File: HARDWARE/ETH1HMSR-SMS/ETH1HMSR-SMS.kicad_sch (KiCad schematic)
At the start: 5 parts

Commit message: SW and HW development
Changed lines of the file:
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@@
     )
   )
-  (sheet (at 122.555 99.06) (size 104.14 30.48) (fields_autoplaced)
+  (sheet (at 84.455 99.06) (size 142.24 30.48) (fields_autoplaced)
     (stroke (width 0.1524) (type solid))
     (fill (color 0 0 0 0.0000))
-    (property "Sheetname" "Power" (at 122.555 98.3484 0)
+    (property "Sheetname" "Power" (at 84.455 98.3484 0)
       (effects (font (size 1.27 1.27)) (justify left bottom))
     )
-    (property "Sheetfile" "Power.kicad_sch" (at 122.555 130.1246 0)
+    (property "Sheetfile" "Power.kicad_sch" (at 84.455 130.1246 0)
       (effects (font (size 1.27 1.27)) (justify left top))
     )

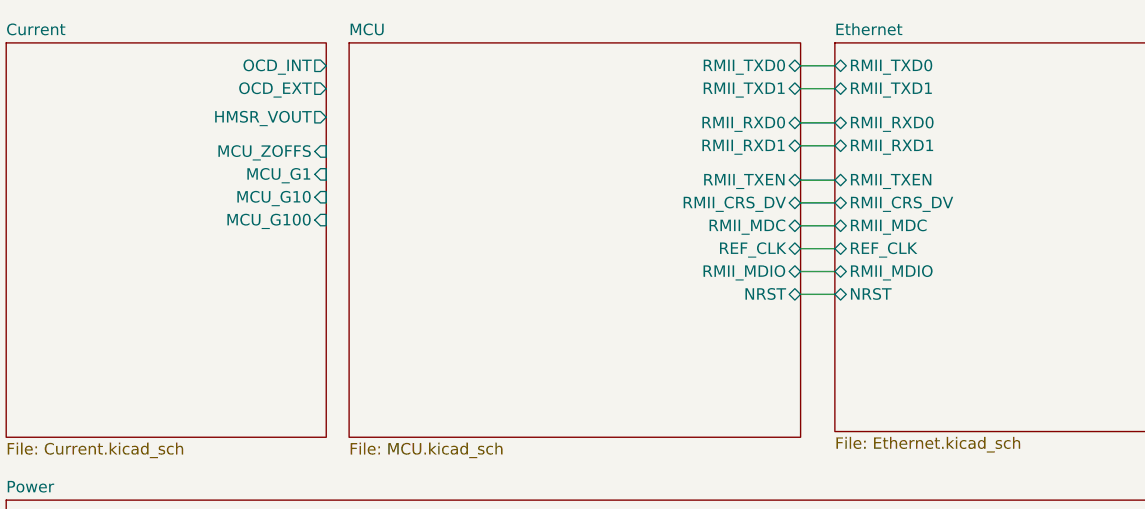
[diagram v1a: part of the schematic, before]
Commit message: Updated to Kicad 8
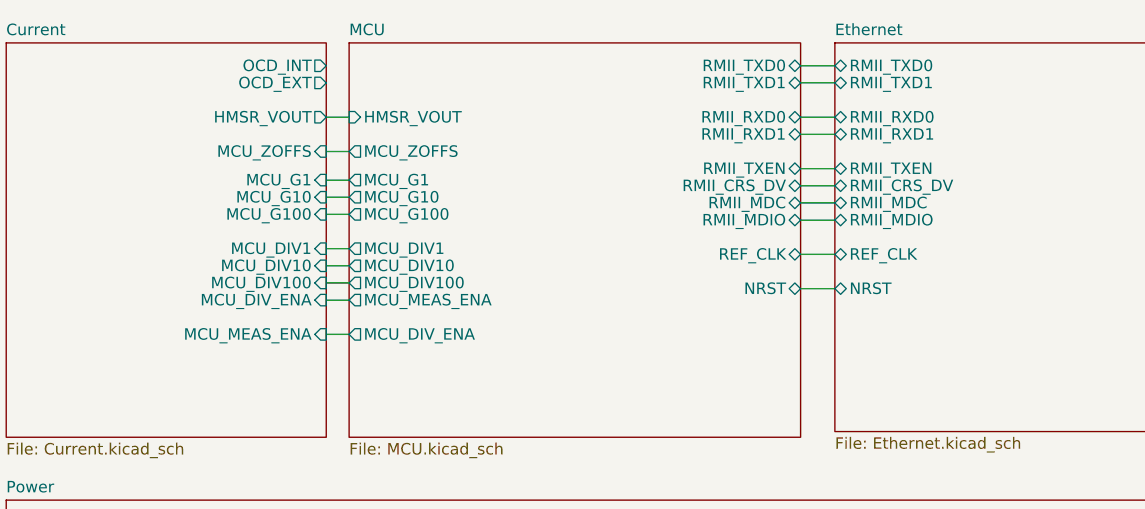
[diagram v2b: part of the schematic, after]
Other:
- sheet Current ports: added MCU_DIV1, MCU_DIV10, MCU_DIV100, MCU_DIV_ENA, MCU_MEAS_ENA; removed none
- sheet MCU ports: added HMSR_VOUT, MCU_DIV1, MCU_DIV10, MCU_DIV100, MCU_DIV_ENA, MCU_G1, MCU_G10, MCU_G100, MCU_MEAS_ENA, MCU_ZOFFS; removed none

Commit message: Development
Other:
- sheet MCU ports: added OCD_EXT, OCD_INT; removed none

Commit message: Development
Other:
- sheet Current ports: added VOUT; removed HMSR_VOUT, MCU_DIV1, MCU_DIV10, MCU_DIV100, MCU_DIV_ENA, MCU_MEAS_ENA
- sheet MCU ports: added VOUT; removed HMSR_VOUT, MCU_DIV1, MCU_DIV10, MCU_DIV100, MCU_DIV_ENA, MCU_MEAS_ENA
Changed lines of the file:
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@@
-	(wire
-		(pts
-			(xy 118.11 78.74) (xy 121.92 78.74)
-		)
-		(stroke
-			(width 0)
-			(type default)
-		)
-	)
 	(wire
 		(pts
@@
 	(wire
 		(pts
-			(xy 118.11 76.2) (xy 121.92 76.2)
-		)
-		(stroke
-			(width 0)
-			(type default)
-		)
-	)
-	(wire
-		(pts
 			(xy 171.45 72.39) (xy 179.07 72.39)
 		)
@@
 	(wire
 		(pts
-			(xy 118.11 71.12) (xy 121.92 71.12)
-		)
-		(stroke
-			(width 0)
-			(type default)
-		)
-	)
-	(wire
-		(pts
 			(xy 171.45 63.5) (xy 179.07 63.5)
 		)
@@
 	(wire
 		(pts
-			(xy 118.11 81.28) (xy 121.92 81.28)
-		)
-		(stroke
-			(width 0)
-			(type default)
-		)
-	)
-	(wire
-		(pts
 			(xy 118.11 63.5) (xy 121.92 63.5)
 		)
@@
 		(pts
 			(xy 171.45 55.88) (xy 179.07 55.88)
-		)
-		(stroke
-			(width 0)
-			(type default)
-		)
-	)
-	(wire
-		(pts
-			(xy 118.11 73.66) (xy 121.92 73.66)
 		)
 		(stroke
@@
 			)
 		)
-		(pin "HMSR_VOUT" output
+		(pin "VOUT" output
 			(at 118.11 57.15 0)
 			(effects
@@
 		(pin "MCU_G100" input
 			(at 118.11 68.58 0)
-			(effects
-				(font
-					(size 1.27 1.27)
-				)
-				(justify right)
-			)
-		)
-		(pin "MCU_DIV10" input
-			(at 118.11 73.66 0)
-			(effects
-				(font
-					(size 1.27 1.27)
-				)
-				(justify right)
-			)
-		)
-		(pin "MCU_DIV100" input
-			(at 118.11 76.2 0)
-			(effects
-				(font
-					(size 1.27 1.27)
-				)
-				(justify right)
-			)
-		)
-		(pin "MCU_DIV1" input
-			(at 118.11 71.12 0)
-			(effects
-				(font
-					(size 1.27 1.27)
-				)
-				(justify right)
-			)
-		)
-		(pin "MCU_DIV_ENA" input
-			(at 118.11 78.74 0)
-			(effects
-				(font
-					(size 1.27 1.27)
-				)
-				(justify right)
-			)
-		)
-		(pin "MCU_MEAS_ENA" input
-			(at 118.11 81.28 0)
 			(effects
 				(font
@@
 			)
 		)
-		(pin "HMSR_VOUT" input
+		(pin "VOUT" input
 			(at 121.92 57.15 180)
-			(effects
-				(font
-					(size 1.27 1.27)
-				)
-				(justify left)
-			)
-		)
-		(pin "MCU_DIV_ENA" output
-			(at 121.92 78.74 180)
 			(effects
 				(font
@@
 			)
 		)
-		(pin "MCU_MEAS_ENA" output
-			(at 121.92 81.28 180)
-			(effects
-				(font
-					(size 1.27 1.27)
-				)
-				(justify left)
-			)
-		)
 		(pin "MCU_G1" output
 			(at 121.92 63.5 180)
@@
 			(effects
 				(font
-					(size 1.27 1.27)
-				)
-				(justify left)
-			)
-		)
-		(pin "MCU_DIV10" output
-			(at 121.92 73.66 180)
-			(effects
-				(font
-					(size 1.27 1.27)
-				)
-				(justify left)
-			)
-		)
-		(pin "MCU_DIV1" output
-			(at 121.92 71.12 180)
-			(effects
-				(font
-					(size 1.27 1.27)
-				)
-				(justify left)
-			)
-		)
-		(pin "MCU_DIV100" output
-			(at 121.92 76.2 180)
-			(effects
-				(font
